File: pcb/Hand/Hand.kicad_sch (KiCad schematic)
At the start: 39 parts, among them J10 Conn_01x03_HALL_7, J11 Conn_01x03_HALL_8, J12 Conn_01x03_HALL_9, J13 Conn_01x03_HALL_10, J14 Conn_01x03_HALL_11, J15 Conn_01x03_HALL_12, J16 Conn_01x03_HALL_13, J17 Conn_01x03_HALL_14, J18 Conn_01x03_HALL_15, J19 Conn_01x05_HAPTIC_1, J2 Conn_01x03_HALL_0, J20 Conn_01x05_HAPTIC_2, J21 Conn_01x05_HAPTIC_3, J22 Conn_01x05_HAPTIC_4, J23 Conn_01x03_FEEDBACK_0, J24 Conn_01x03_FEEDBACK_1, J25 Conn_01x03_FEEDBACK_2, J26 Conn_01x03_FEEDBACK_3, J27 Conn_01x03_FEEDBACK_4, J28 Conn_01x03_SPOOLPOT_1, J29 Conn_01x03_SPOOLPOT_2, J3 Conn_01x05_HAPTIC_0, J30 Conn_01x03_SPOOLPOT_3, J31 Conn_01x03_SPOOLPOT_0, J32 Conn_01x03_SPOOLPOT_4, J33 Conn_01x12_Ribbon_Top, J34 Conn_01x12_Ribbon_Bottom, J35 Conn_01x02_Feedback_Power, J4 Conn_01x03_HALL_1, J5 Conn_01x03_HALL_2, J6 Conn_01x03_HALL_3, J7 Conn_01x03_HALL_4, J8 Conn_01x03_HALL_5, J9 Conn_01x03_HALL_6, U1 CD74HC4067M96, U2 4754, U3 TCA9548A

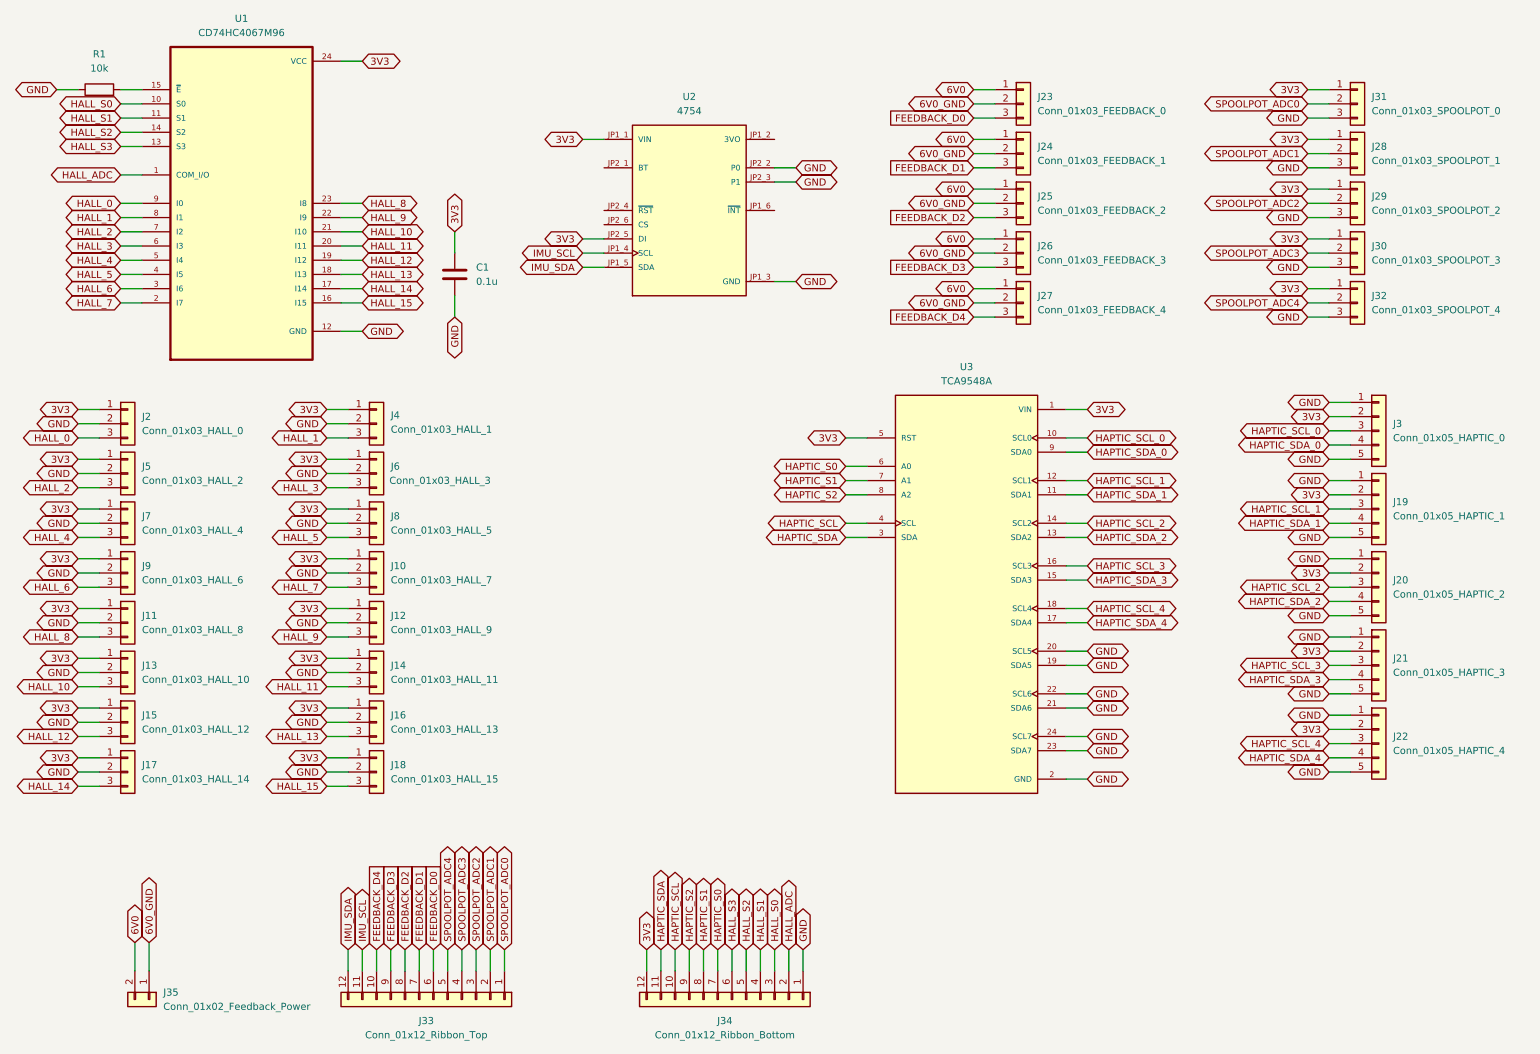
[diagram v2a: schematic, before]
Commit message: updated and routed hand pcb
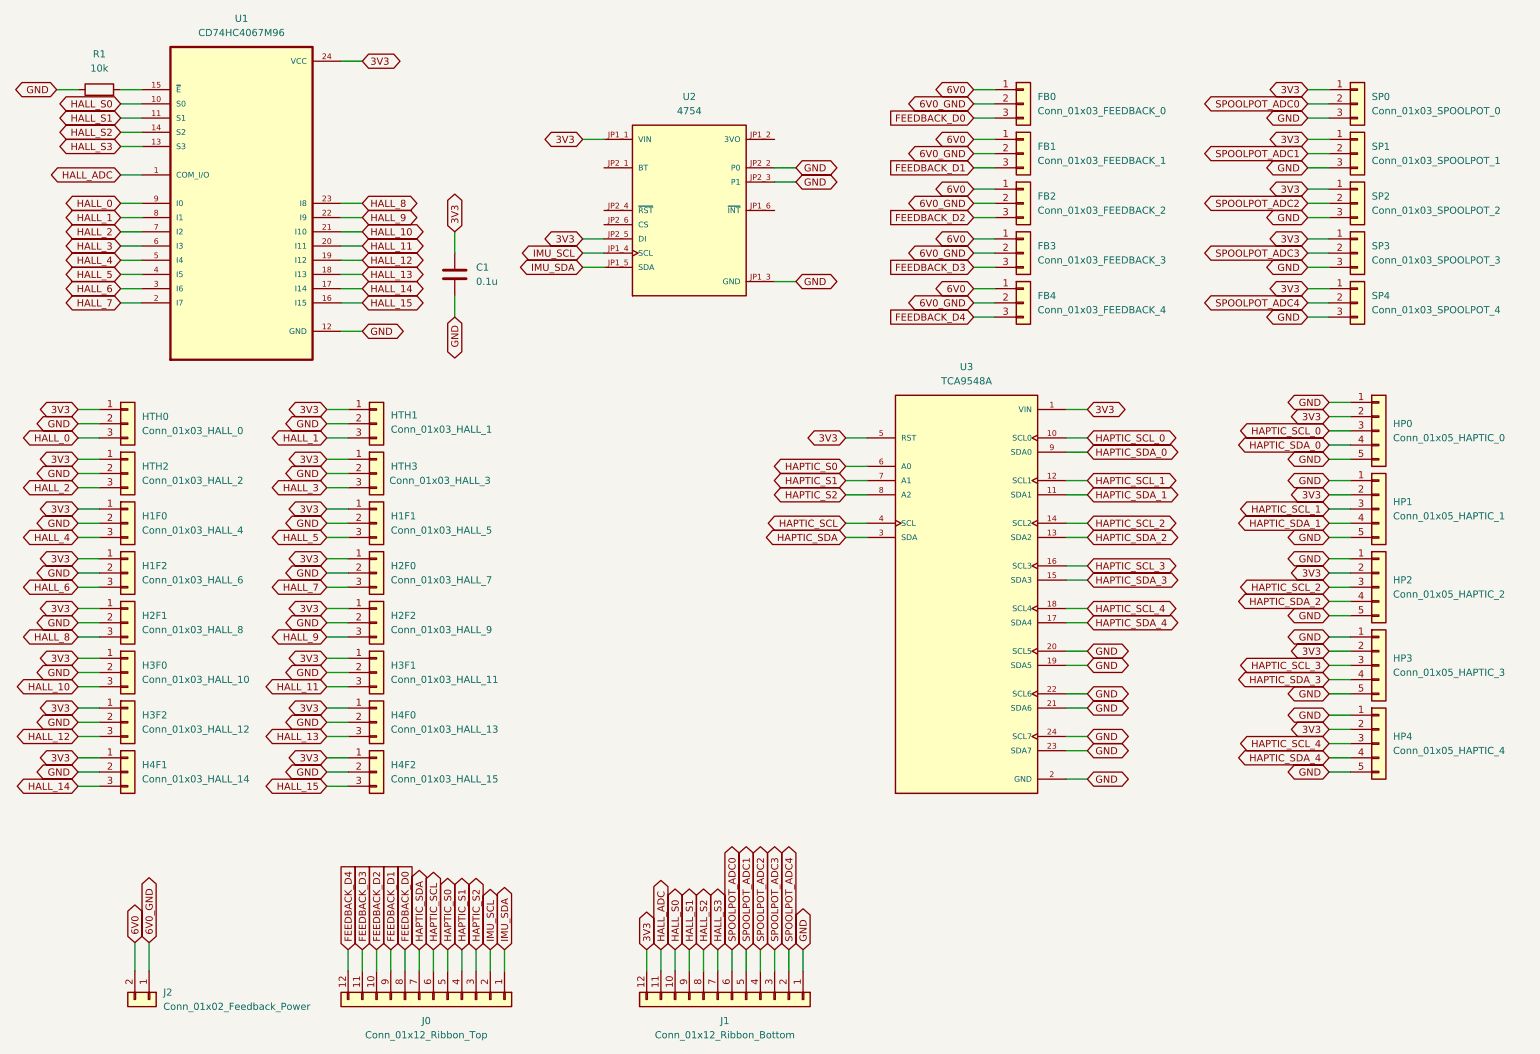
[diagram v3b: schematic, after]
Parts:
- C1: footprint Capacitor_THT:CP_Radial_D5.0mm_P2.50mm -> Capacitor_SMD:C_1206_3216Metric
- J2: renamed from J35; footprint Connector_PinHeader_2.54mm:PinHeader_1x02_P2.54mm_Vertical_SMD_Pin1Left -> Connector_PinHeader_2.54mm:PinHeader_1x02_P2.54mm_Vertical
- R1: footprint Resistor_THT:R_Axial_DIN0207_L6.3mm_D2.5mm_P10.16mm_Horizontal -> Resistor_SMD:R_0402_1005Metric
- renumbered J23 to FB0, J24 to FB1, J25 to FB2, J26 to FB3, J27 to FB4, J7 to H1F0, J8 to H1F1, J9 to H1F2, J10 to H2F0, J11 to H2F1, J12 to H2F2, J13 to H3F0, J14 to H3F1, J15 to H3F2, J16 to H4F0, J17 to H4F1, J18 to H4F2, J3 to HP0, J19 to HP1, J20 to HP2, J21 to HP3, J22 to HP4, J2 to HTH0, J4 to HTH1, J5 to HTH2, J6 to HTH3, J33 to J0, J34 to J1, J31 to SP0, J28 to SP1, J29 to SP2, J30 to SP3, J32 to SP4
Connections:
- net FEEDBACK_D0: now also J0.8 (Pin_8); no longer J0.6 (Pin_6)
- net FEEDBACK_D1: now also J0.9 (Pin_9); no longer J0.7 (Pin_7)
- net FEEDBACK_D2: now also J0.10 (Pin_10); no longer J0.8 (Pin_8)
- net FEEDBACK_D3: now also J0.11 (Pin_11); no longer J0.9 (Pin_9)
- net FEEDBACK_D4: now also J0.12 (Pin_12); no longer J0.10 (Pin_10)
- net HALL_ADC: now also J1.11 (Pin_11); no longer J1.2 (Pin_2)
- net HALL_S0: now also J1.10 (Pin_10); no longer J1.3 (Pin_3)
- net HALL_S1: now also J1.9 (Pin_9); no longer J1.4 (Pin_4)
- net HALL_S2: now also J1.8 (Pin_8); no longer J1.5 (Pin_5)
- net HALL_S3: now also J1.7 (Pin_7); no longer J1.6 (Pin_6)
- net HAPTIC_S0: now also J0.5 (Pin_5); no longer J1.7 (Pin_7)
- net HAPTIC_S1: now also J0.4 (Pin_4); no longer J1.8 (Pin_8)
- net HAPTIC_S2: now also J0.3 (Pin_3); no longer J1.9 (Pin_9)
- net HAPTIC_SCL: now also J0.6 (Pin_6); no longer J1.10 (Pin_10)
- net HAPTIC_SDA: now also J0.7 (Pin_7); no longer J1.11 (Pin_11)
- net IMU_SCL: now also J0.2 (Pin_2); no longer J0.11 (Pin_11)
- net IMU_SDA: now also J0.1 (Pin_1); no longer J0.12 (Pin_12)
- net SPOOLPOT_ADC0: now also J1.6 (Pin_6); no longer J0.1 (Pin_1)
- net SPOOLPOT_ADC1: now also J1.5 (Pin_5); no longer J0.2 (Pin_2)
- net SPOOLPOT_ADC2: now also J1.4 (Pin_4); no longer J0.3 (Pin_3)
- net SPOOLPOT_ADC3: now also J1.3 (Pin_3); no longer J0.4 (Pin_4)
- net SPOOLPOT_ADC4: now also J1.2 (Pin_2); no longer J0.5 (Pin_5)
